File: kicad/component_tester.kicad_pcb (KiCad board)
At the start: 2 copper layers, 100.4 x 83 mm, 86 parts, among them IC201 MCP1640, IC202 ATmega328P-MMH, IC301 FT232RL, IC302 MAX1811, J301 0R-JUMPA, J302 0R-JUMPA, Q201 8 MHz, Q401 BSS138, Q402 BSS138, SW201 TASTER-RACON8SMD, T201 PMV65XP, T202 BSS84, T203 BSS123, T204 BC847, T301 BSS123, U401 VREG_SOT23-5, X201 MICRO-USB, X202 ISP

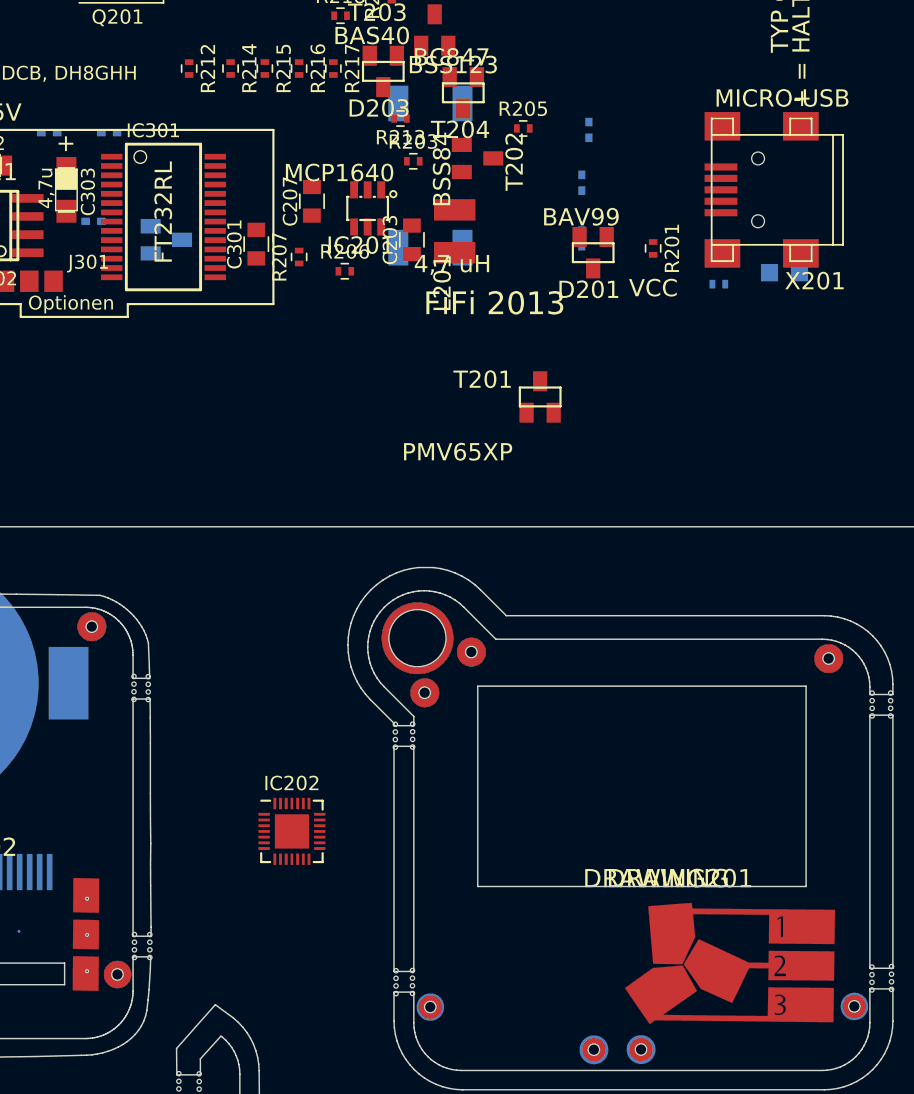
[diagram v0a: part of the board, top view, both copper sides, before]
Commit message: Switch button footprint
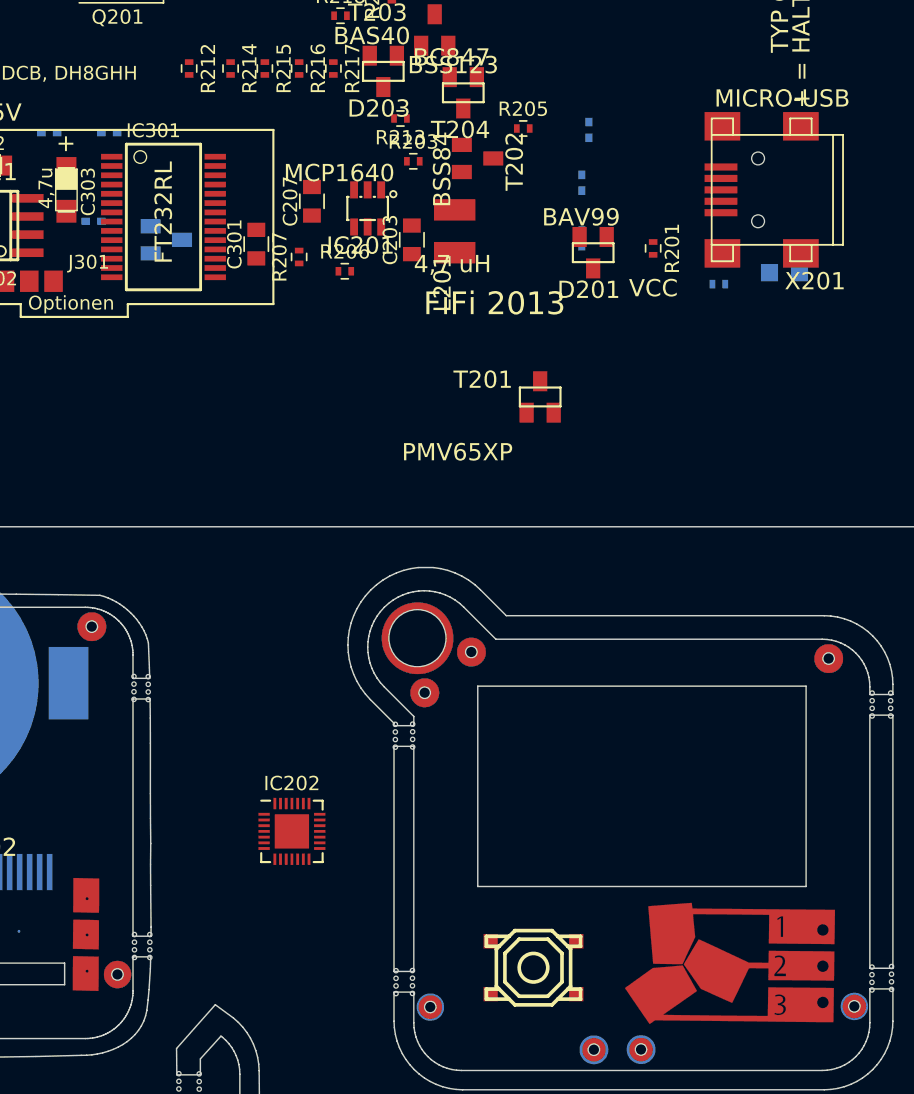
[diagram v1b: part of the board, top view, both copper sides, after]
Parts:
- SW201: value TASTER-RACON8SMD -> Tactile Switch; footprint component_tester:TASTER-RACON8SMD -> smisioto.eu/kicad_libs/modules/w_switch.pretty:smd_push2; moved to F.Cu
- moved SW201 56.0 mm to (160.2, 107.5)

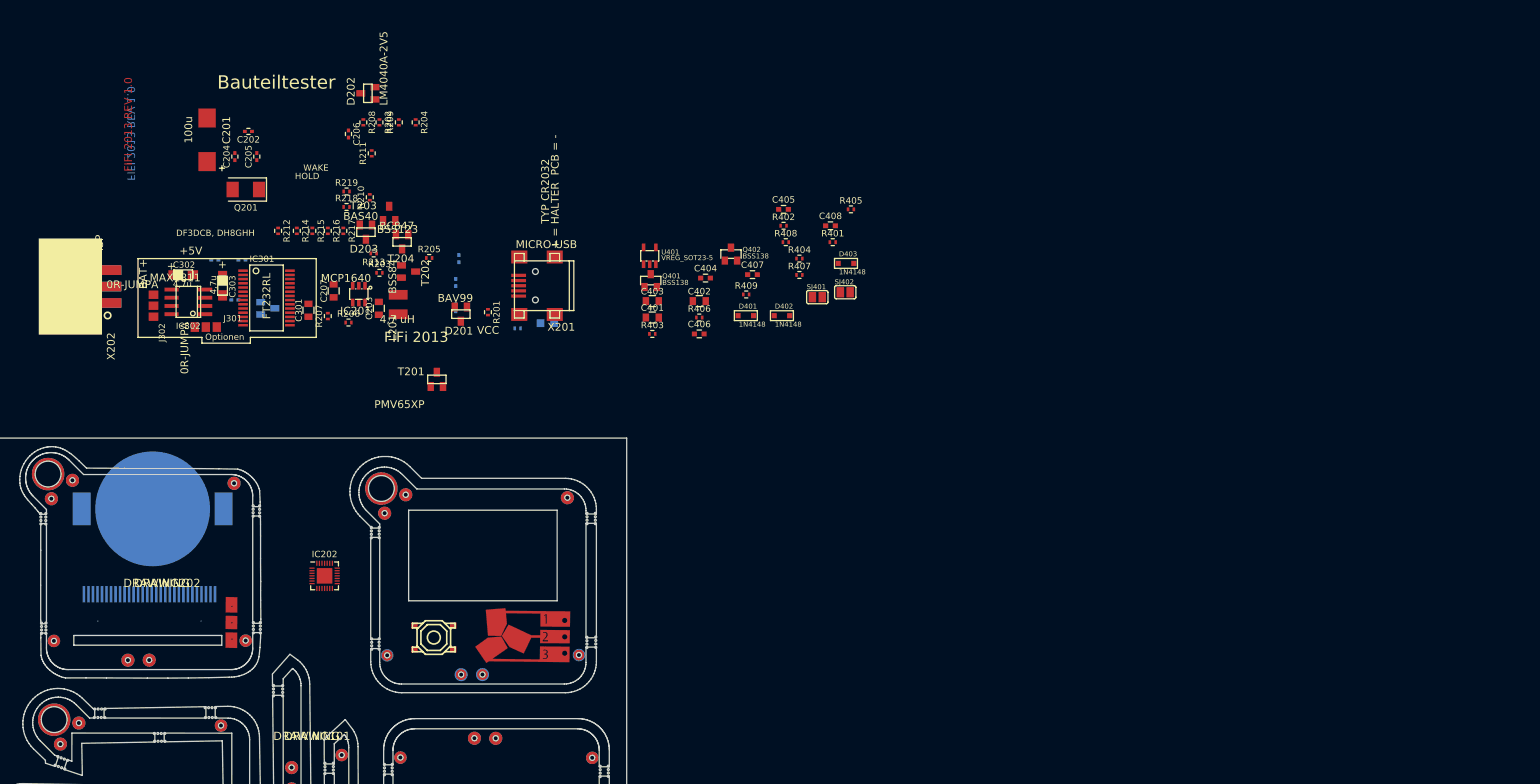
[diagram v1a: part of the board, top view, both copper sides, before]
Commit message: Flip the board and begin placing
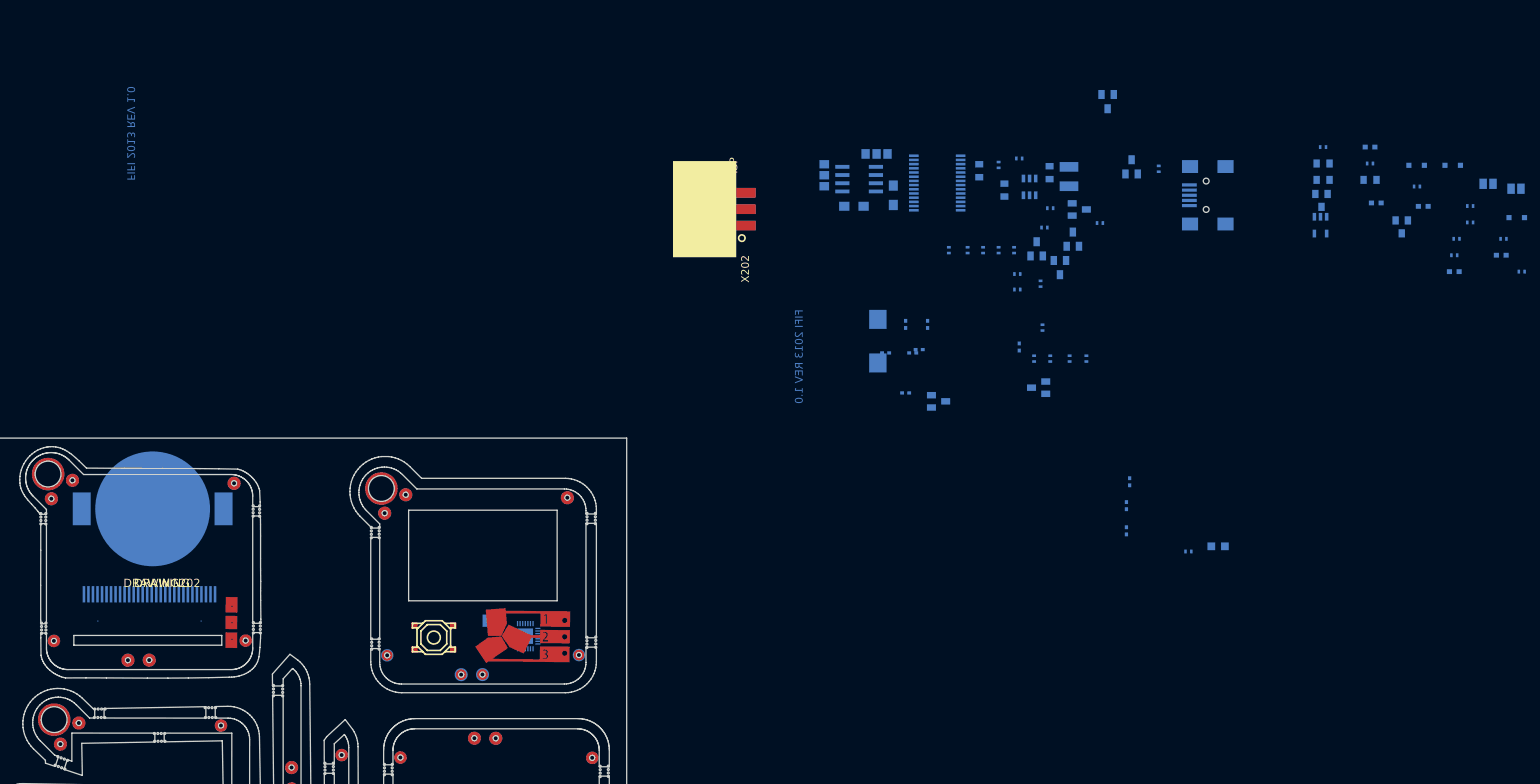
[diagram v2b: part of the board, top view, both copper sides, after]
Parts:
- C201, C202, C203, C204, C205, C206, C207, C301, C302, C303, C401, C402, C403, C404, C405, C406, C407, C408, D201, D202, D203, D401, D402, D403, IC201, IC202, IC301, IC302, J301, J302, L201, Q201, Q401, Q402, R201, R202, R203, R204, R205, R206, R207, R208, R209, R210, R211, R212, R213, R214, R215, R216, R217, R218, R219, R401, R402, R403, R404, R405, R406, R407, R408, R409, SJ401, SJ402, T201, T202, T203, T204, U401, X201: moved to B.Cu
- moved D202 113.4 mm to (253.8, 68.8), turned to 270 degrees
- moved T201 112.4 mm to (264.5, 24.5)
- moved R202 110.1 mm to (255.6, 64.3), turned to 90 degrees
- moved R204 110.1 mm to (261.2, 64.3), turned to 90 degrees
- moved R208 110.1 mm to (253.1, 64.3), turned to 90 degrees
- moved R209 110.1 mm to (258.6, 64.3), turned to 270 degrees
- moved C211 109.5 mm to (267.9, 83.4)
- moved C212 109.5 mm to (267.4, 87.1)
- moved C213 109.5 mm to (267.4, 91.0)
- moved R301 109.5 mm to (277.0, 94.2)
- moved LED301 109.5 mm to (281.6, 93.4)
- moved C202 109.2 mm to (235.3, 62.9)
- moved C206 109.0 mm to (250.8, 62.5), turned to 90 degrees
- moved C201 108.5 mm to (228.9, 61.6), turned to 90 degrees
- moved C406 107.8 mm to (305.2, 31.5)
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
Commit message: Use hierplace to re-arrange footprints
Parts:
- moved R401 186.3 mm to (139.8, 55.2)
- moved D403 183.6 mm to (144.8, 56.4)
- moved C408 181.2 mm to (144.4, 52.1)
- moved R402 178.7 mm to (139.8, 57.1)
- moved SJ402 176.6 mm to (152.8, 62.4)
- moved SJ401 176.6 mm to (148.7, 62.4)
- moved D402 174.9 mm to (144.8, 58.7)
- moved R405 172.7 mm to (156.2, 60.1)
- moved Q402 170.4 mm to (140.6, 61.9)
- moved C405 169.6 mm to (148.8, 56.5)
- moved R404 165.8 mm to (156.1, 62.9)
- moved R409 165.7 mm to (148.2, 59.0)
- moved C407 165.2 mm to (148.8, 54.5)
- moved R407 165.1 mm to (156.2, 55.0)
- moved R408 162.4 mm to (156.3, 52.5)
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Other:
- board text removed: "+ = HALTER PCB = -"
- board text removed: "+5V"
- board text removed: "BAT+"
- board text removed: "Bauteiltester"
- board text removed: "FiFi 2013"
- board text removed: "HOLD"
- board text removed: "Optionen"
- board text removed: "TYP CR2032"
- board text removed: "VCC"
- board text removed: "WAKE"

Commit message: Continue placing
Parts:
- moved DRAWING201 87.5 mm to (169.6, 101.5)
- moved SW201 85.5 mm to (160.6, 107.7)
- moved OLED1 46.3 mm to (115.8, 100.1)
- moved DRAWING202 37.1 mm to (118.1, 99.3)
- moved BAT201 0.36 mm to (116.8, 87.9)
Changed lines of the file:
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@@
   (general
     (thickness 1.6)
-    (drawings 11)
+    (drawings 7)
     (tracks 0)
     (zones 0)
@@
   )
   (module drawings:pads_bottom (layer Top)
-    (at 115.321779 62.302596)
-    (fp_text reference DRAWING202 (at 0 0) (layer F.SilkS)
+    (at 118.069008 99.316929)
+    (fp_text reference DRAWING202 (at 0 0) (layer F.SilkS) hide
       (effects (font (size 1.27 1.27) (thickness 0.15)))
     )
-    (fp_text value DRAWING (at 0 0) (layer F.SilkS)
+    (fp_text value DRAWING (at 0 0) (layer F.SilkS) hide
       (effects (font (size 1.27 1.27) (thickness 0.15)))
     )
@@
   )
   (module drawings:pads (layer Top)
-    (at 106.137625 41.325733)
+    (at 169.629008 101.536929)
     (fp_text reference DRAWING201 (at 0 0) (layer F.SilkS) hide
       (effects (font (size 1.27 1.27) (thickness 0.15)))
@@
   )
   (module smisioto.eu/kicad_libs/modules/w_switch.pretty:smd_push2 (layer Top)
-    (at 111.613502 37.647772 180)
+    (at 160.61 107.72 180)
     (descr "SMD Pushbutton 2")
     (autoplace_cost180 10)
@@
   )
   (module component_tester:SSD1306 (layer Bottom)
-    (at 146.318188 65.289796)
+    (at 115.824 100.076)
     (attr smd)
     (fp_text reference OLED1 (at -3.85 -1.75) (layer B.SilkS)
@@
   )
   (module StefanHamminga/SH_Batteries.pretty:Battery_Retainer_2032_BK-912 (layer Bottom)
-    (at 117.094 87.63 180)
+    (at 116.84 87.884 180)
     (attr smd)
     (fp_text reference BAT201 (at -10.9 -3.7 180) (layer B.SilkS)
@@
       (net 42 "Net-(D203-Pad3)") (solder_mask_margin 0.0762))
   )
-  (gr_arc (start 128.302879 50.973337) (end 126.952879 58.4036) (angle 80.990186) (layer B.Mask) (width 0.15))
-  (gr_arc (start 128.356139 51.103601) (end 121.352879 48.5036) (angle 135.114493) (layer B.Mask) (width 0.15))
-  (gr_arc (start 128.302878 50.921782) (end 135.752879 50.0036) (angle 34.661768) (layer B.Mask) (width 0.15))
-  (gr_arc (start 128.236212 51.0036) (end 131.952879 57.6036) (angle 17.061531) (layer B.Mask) (width 0.15))
-  (gr_circle (center 152.952879 51.0036) (end 158.952879 51.0036) (layer B.Fab) (width 0.4064))
-  (gr_circle (center 128.352879 51.0036) (end 135.852879 51.0036) (layer B.SilkS) (width 0.254))
+  (gr_line (start 131.04 107.98) (end 128.91 107.98) (layer Dwgs.User) (width 0.2))
+  (gr_line (start 182.65 110.21) (end 180.52 110.21) (layer Dwgs.User) (width 0.2))
   (gr_text www.ov-lennestadt.de (at 121.352879 21.7036 -90) (layer B.Mask)
     (effects (font (size 1.2065 1.2065) (thickness 0.1016)) (justify right top mirror))

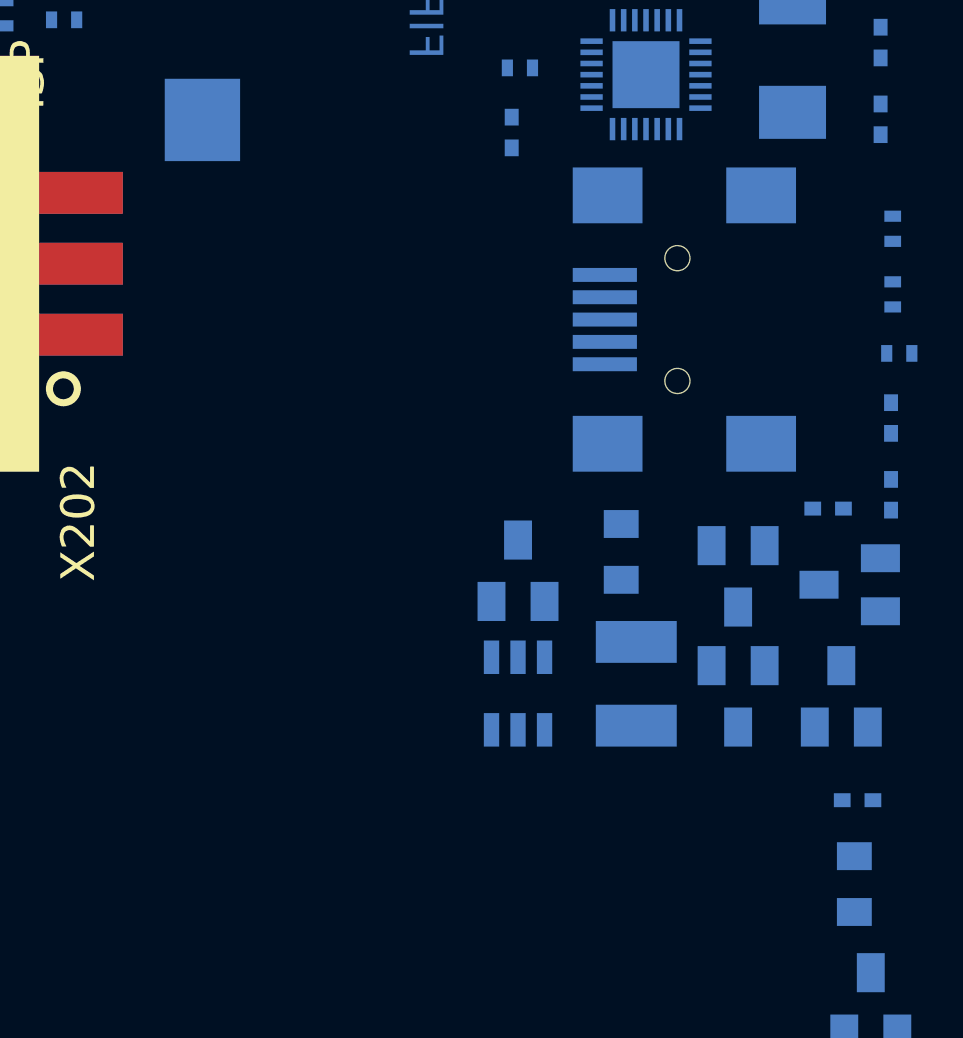
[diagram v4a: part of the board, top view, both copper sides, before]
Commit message: Change USB footprint
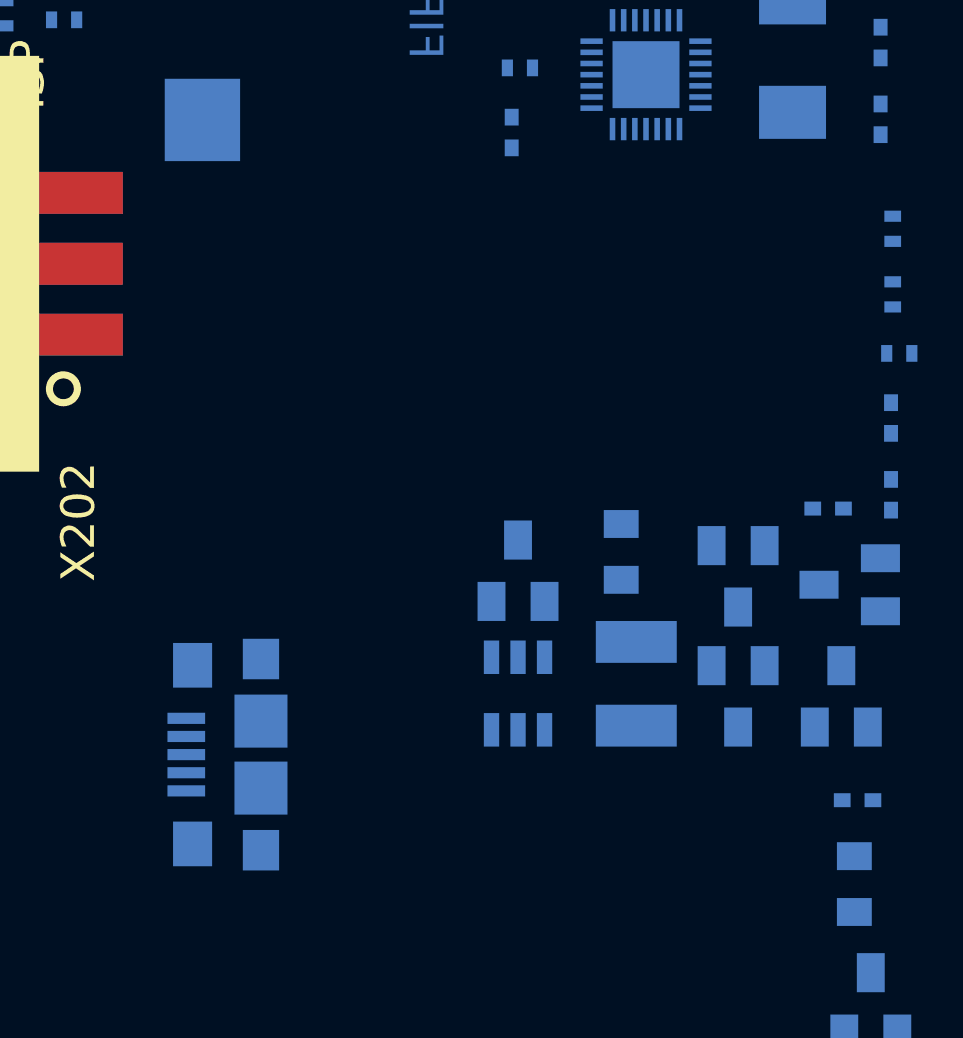
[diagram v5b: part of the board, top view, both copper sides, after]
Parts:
- X201: footprint component_tester:MINI-USB-B5 -> component_tester:TE_1981568-1
- moved X201 23.4 mm to (107.4, 61.6), turned to 270 degrees
